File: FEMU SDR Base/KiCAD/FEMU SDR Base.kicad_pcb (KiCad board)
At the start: 4 copper layers, 164.8 x 164.8 mm, 29 parts, among them P8 Raspi_Power_Shield, U1 TPS562209, U2 SDR_1_LDO_1_2V, U3 SDR_2_LDO_1_2V, U4 SDR_1_LDO_3_3V, U5 SDR_2_LDO_3_3V

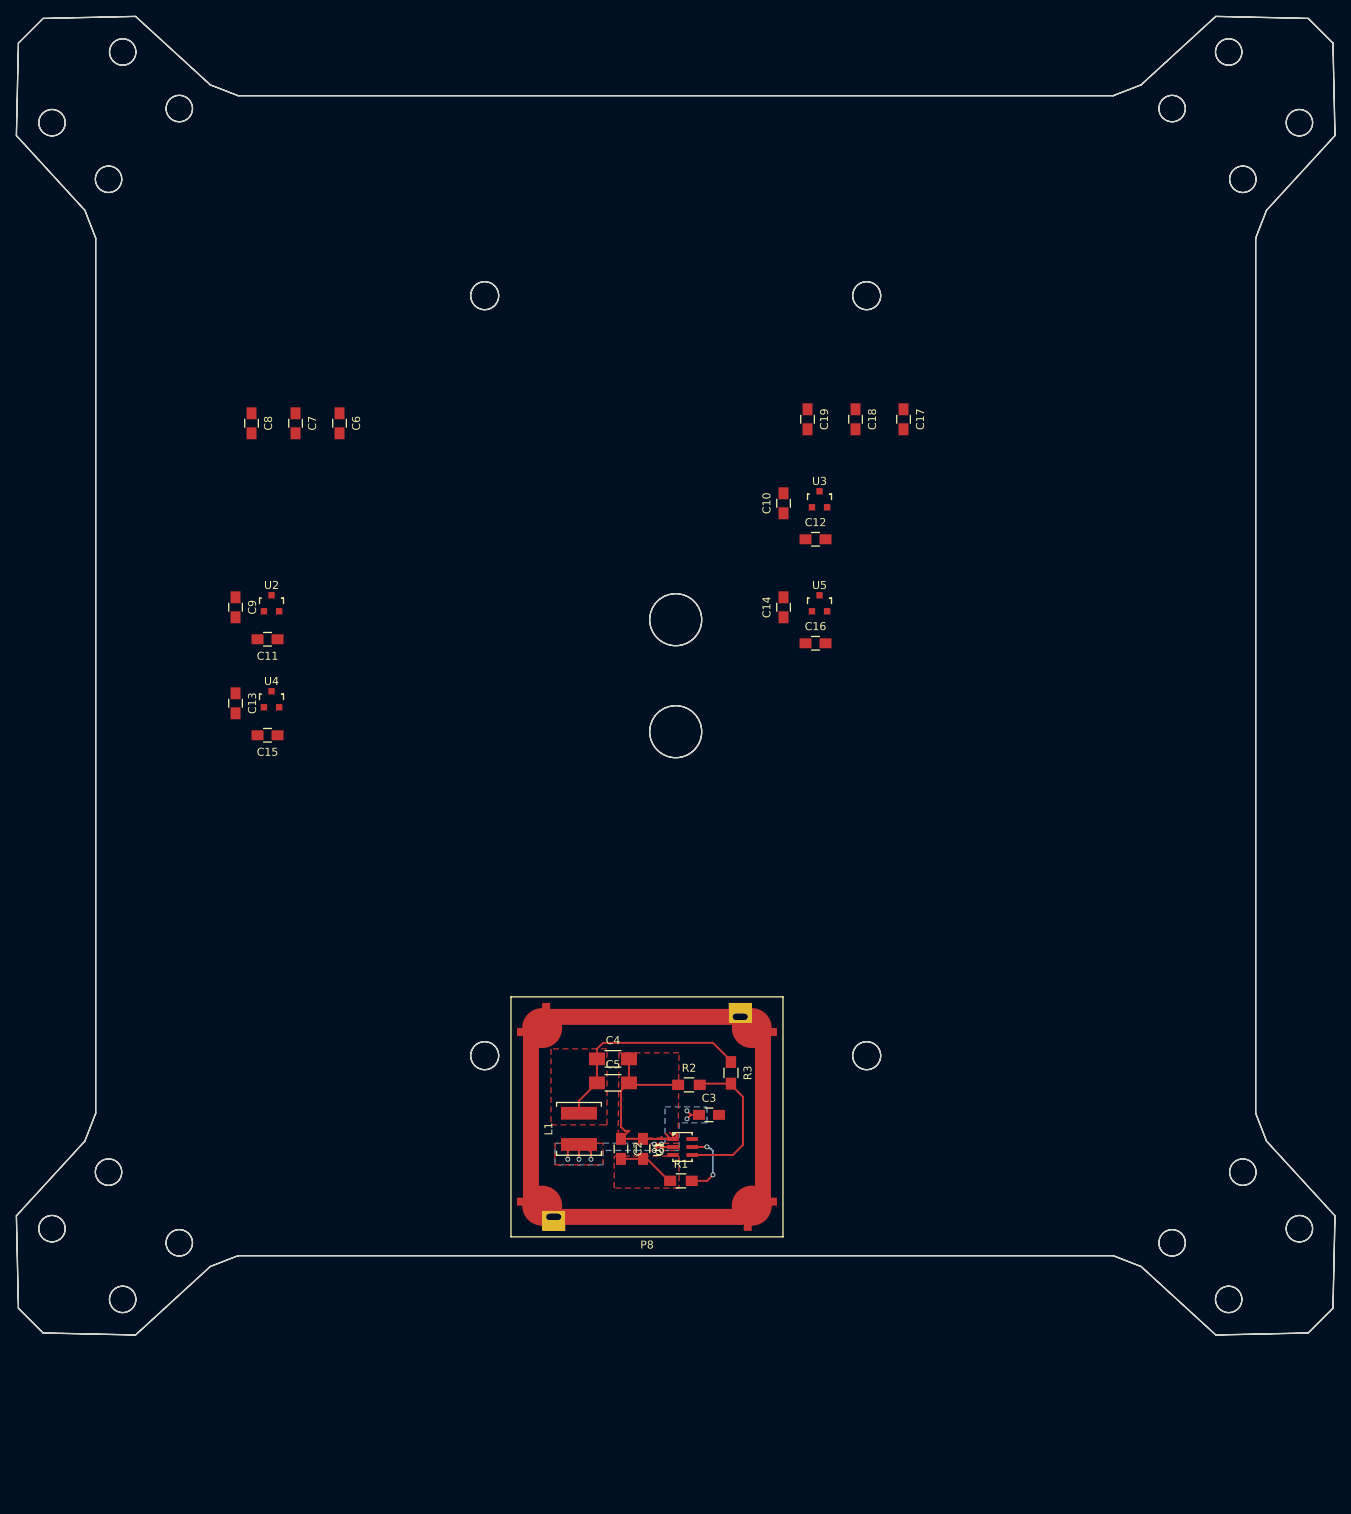
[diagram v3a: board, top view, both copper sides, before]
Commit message: Added SDR shield footprint, updated raspi shield footprints
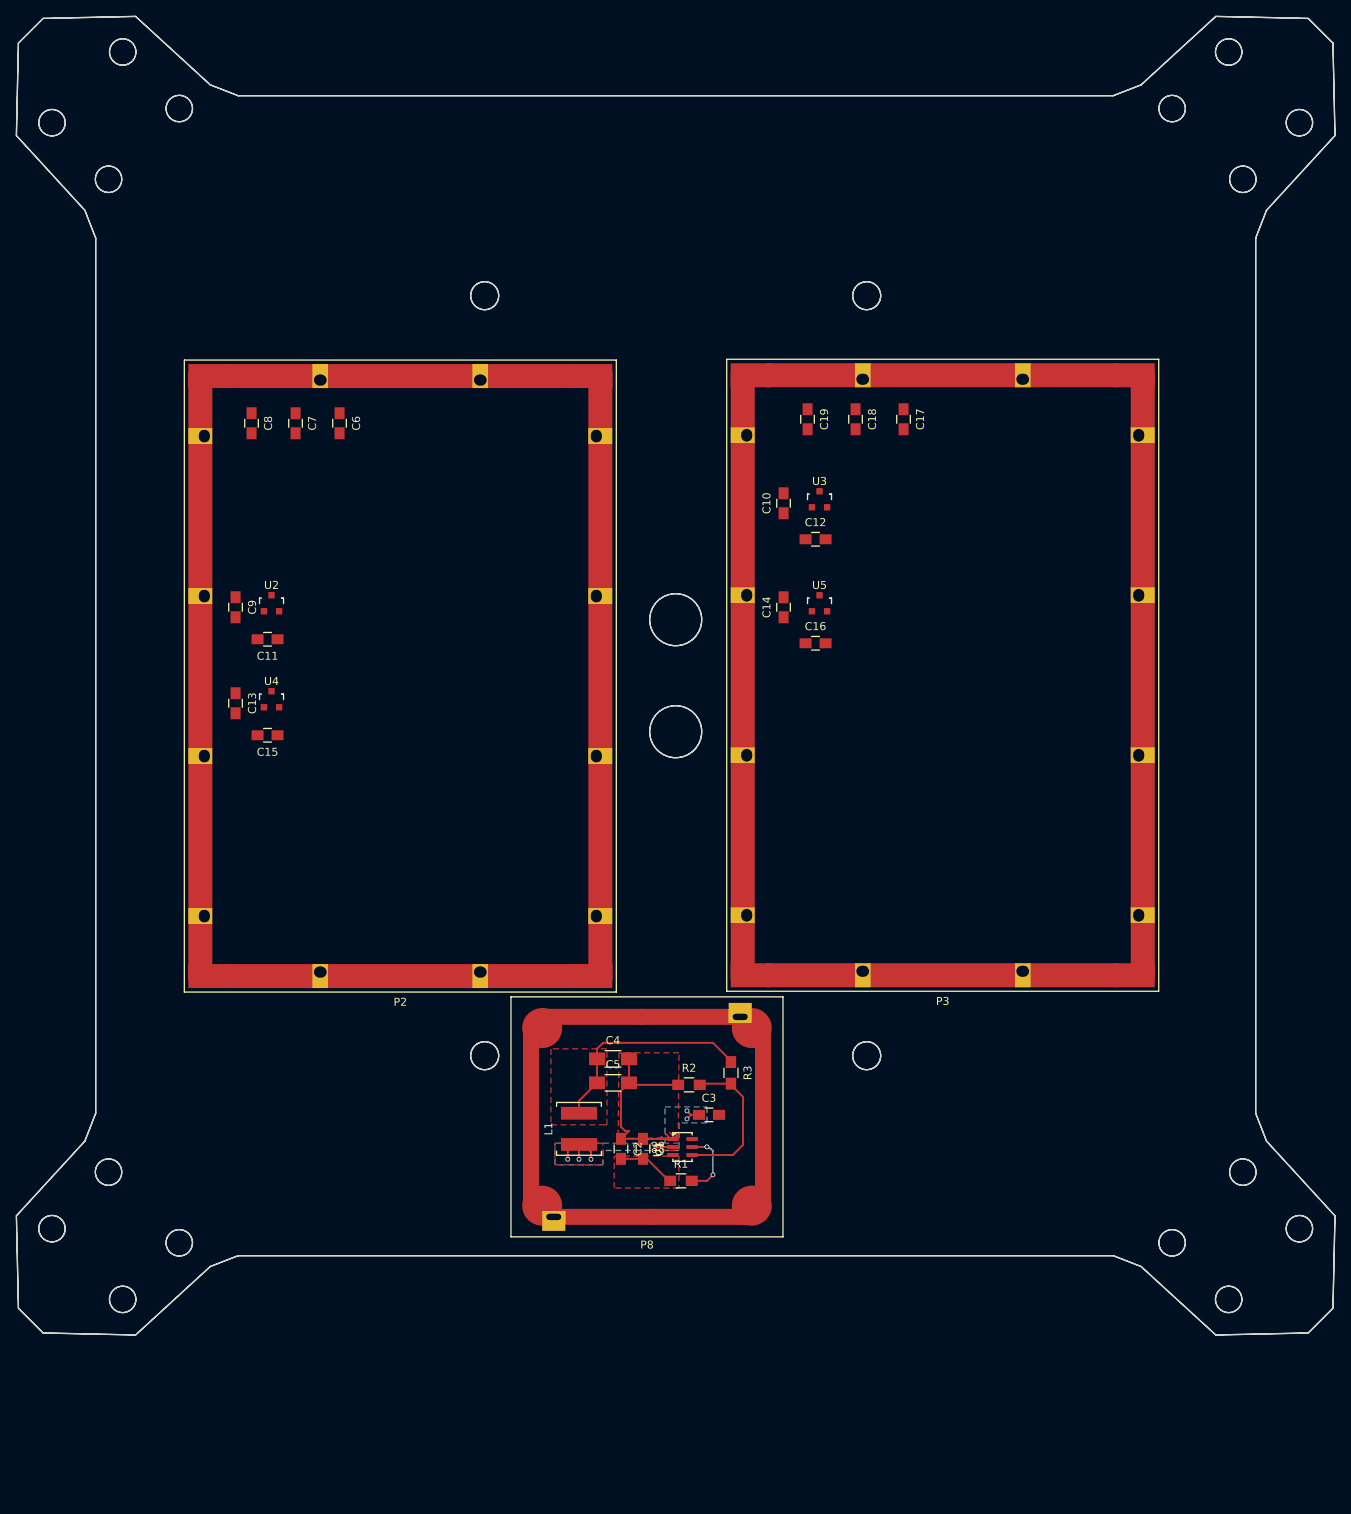
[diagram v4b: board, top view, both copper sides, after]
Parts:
- added P2: SDR_Shield_1, ARB_foots:SDR_Shield_75x50mm, F.Cu at (50.1, 84.6)
- added P3: SDR_Shield_2, ARB_foots:SDR_Shield_75x50mm, F.Cu at (117.9, 84.5)
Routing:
- net GND: track 99.8 -> 10.7 mm

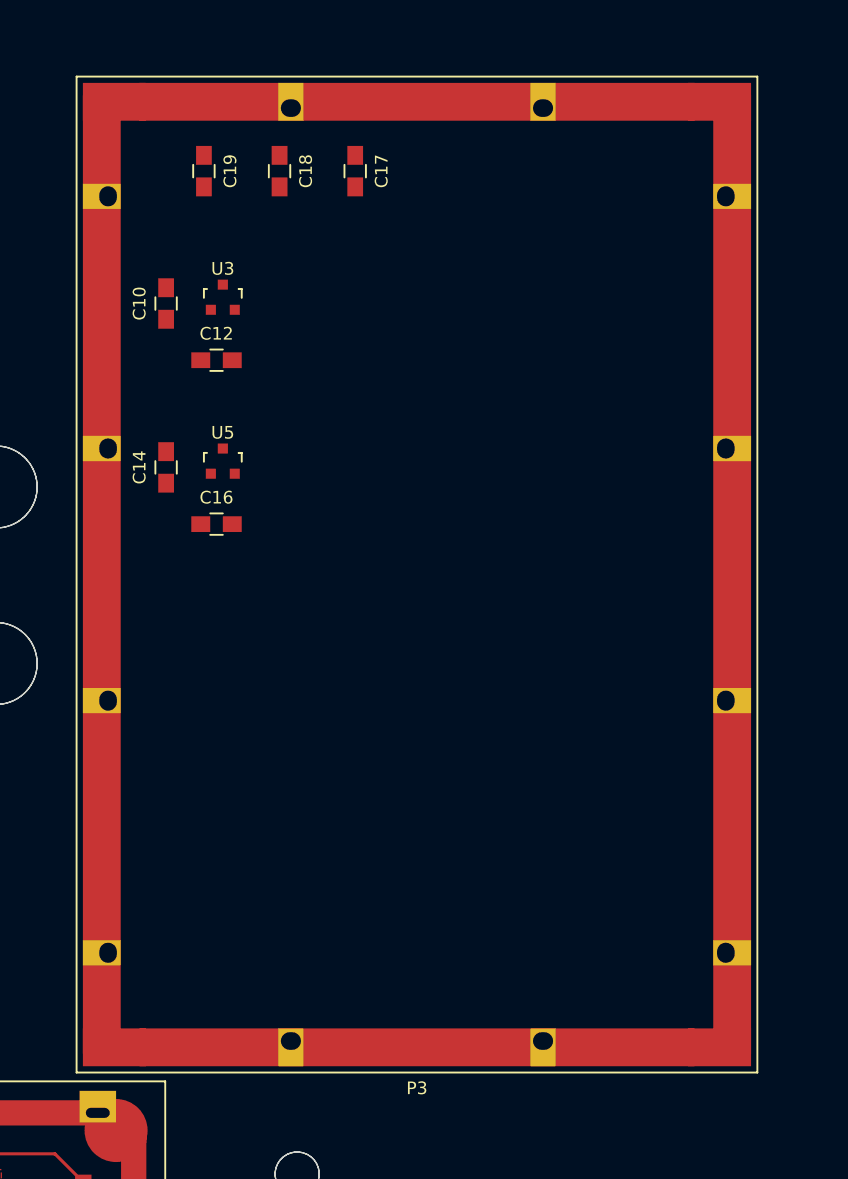
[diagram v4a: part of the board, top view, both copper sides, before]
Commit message: STATUS=FREE, shifted one sdr footprint
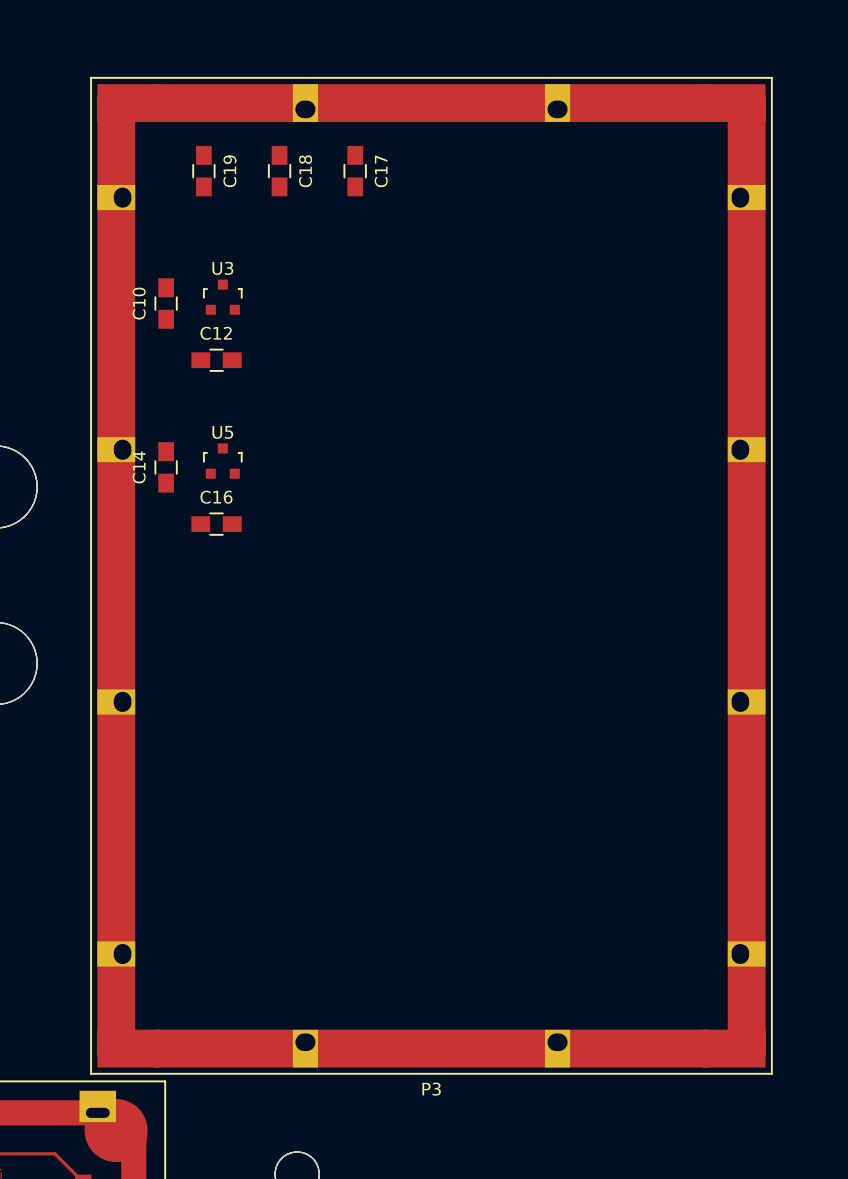
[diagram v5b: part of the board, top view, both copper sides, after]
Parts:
- moved P3 1.15 mm to (119.0, 84.6)
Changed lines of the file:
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@@
     (links 260)
     (no_connects 179)
-    (area 2.059561 2.092061 166.982639 167.015139)
+    (area -15.999999 2.092061 187 174.700001)
     (thickness 1.6)
     (drawings 250)
@@
   )
   (module ARB_foots:SDR_Shield_75x50mm (layer F.Cu)
-    (at 117.9 84.5)
+    (at 119.05 84.6)
     (fp_text reference P3 (at 0 40.75) (layer F.SilkS)
       (effects (font (size 1 1) (thickness 0.15)))

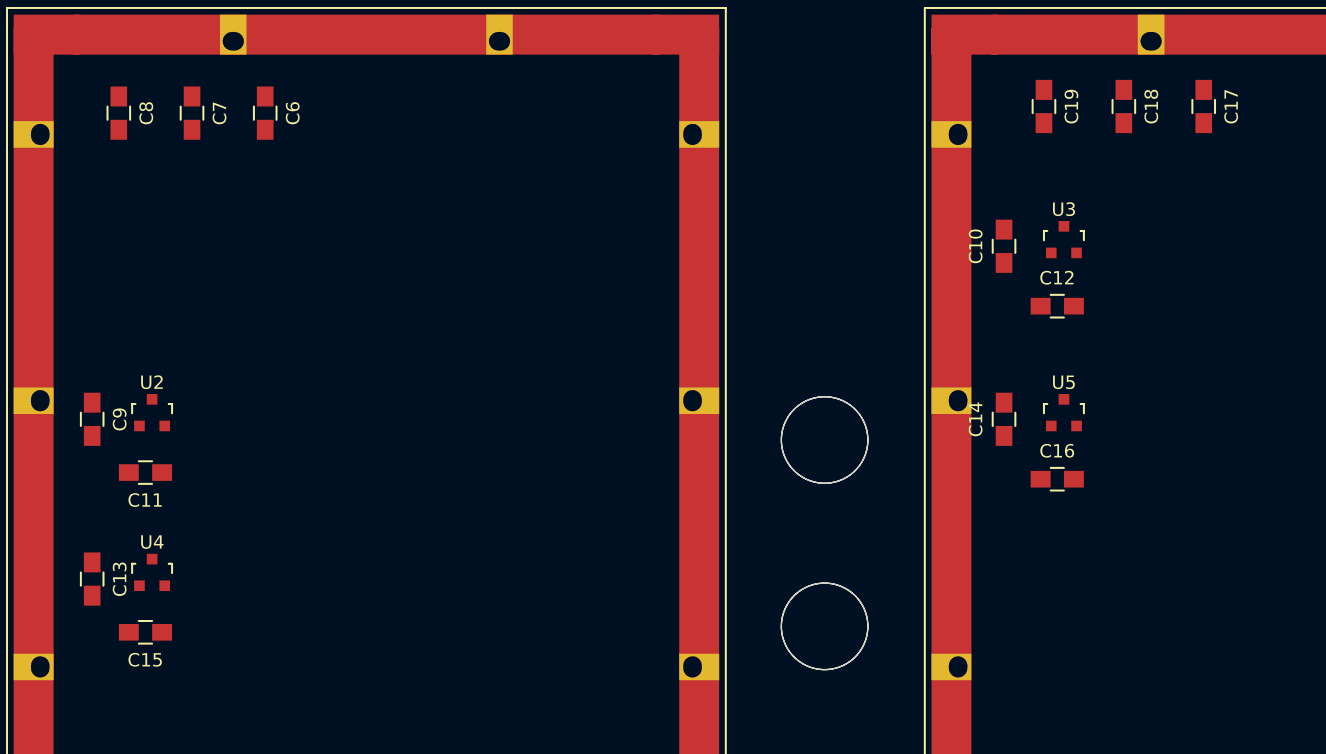
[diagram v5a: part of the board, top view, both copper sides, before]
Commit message: rearranged components in SDR shield footrpint
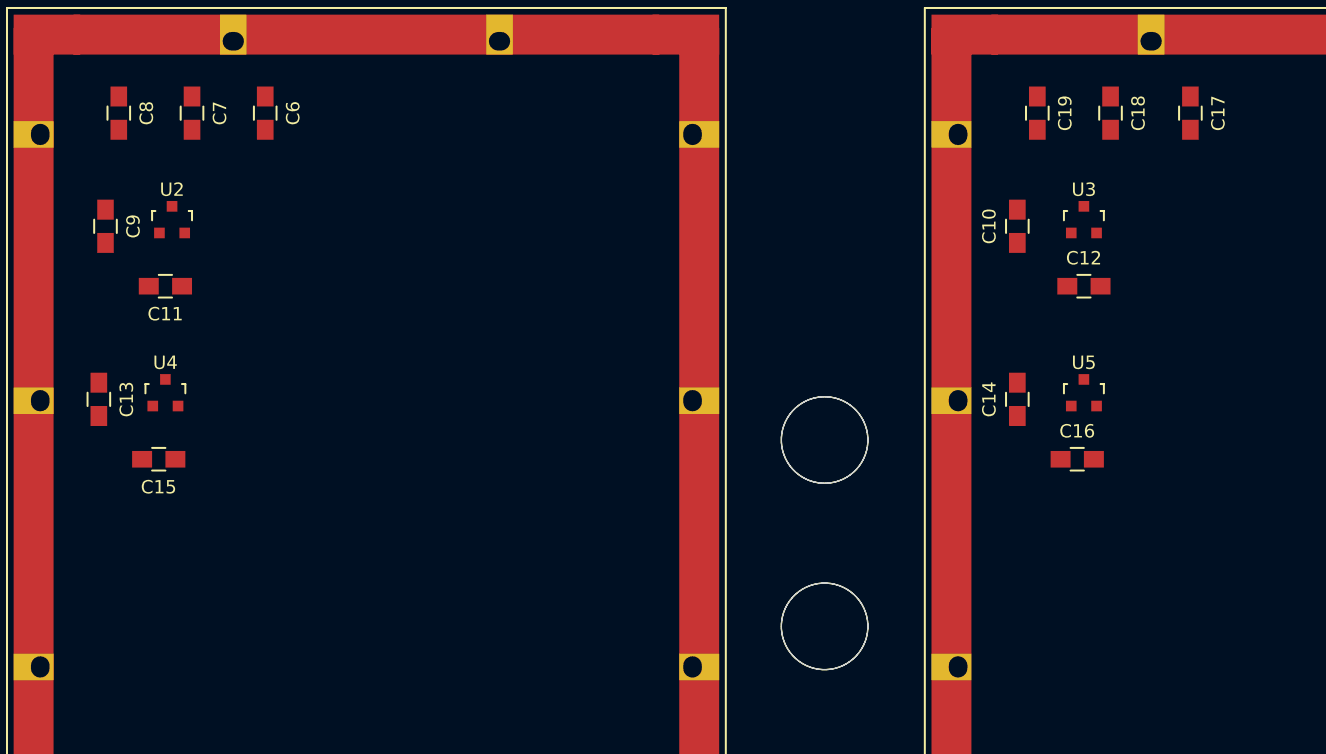
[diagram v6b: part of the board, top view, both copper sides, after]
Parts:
- moved U2 14.6 mm to (35.5, 61.0)
- moved C9 14.5 mm to (30.5, 61.5)
- moved C11 14.1 mm to (35.0, 66.0)
- moved U4 13.5 mm to (35.0, 74.0)
- moved C13 13.5 mm to (30.0, 74.5)
- moved C15 13.0 mm to (34.5, 79.0)
- moved C12 2.50 mm to (104.0, 66.0)
- moved C16 2.12 mm to (103.5, 79.0)
- moved U3 2.12 mm to (104.0, 61.0)
- moved U5 2.12 mm to (104.0, 74.0)
- moved C10 1.80 mm to (99.0, 61.5)
- moved C14 1.80 mm to (99.0, 74.5)
- moved C17 1.12 mm to (112.0, 53.0)
- moved C18 1.12 mm to (106.0, 53.0)
- moved C19 0.71 mm to (100.5, 53.0)
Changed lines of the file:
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@@
   )
   (module TO_SOT_Packages_SMD:SOT-23 (layer F.Cu)
-    (at 34 75.5)
+    (at 35.5 61)
     (descr "SOT-23, Standard")
     (tags SOT-23)
@@
   )
   (module TO_SOT_Packages_SMD:SOT-23 (layer F.Cu)
-    (at 102.5 62.5)
+    (at 104 61)
     (descr "SOT-23, Standard")
     (tags SOT-23)
@@
       (effects (font (size 1 1) (thickness 0.15)))
     )
-    (fp_text value SDR_2_LDO_1_2V (at 0 -5) (layer F.Fab)
+    (fp_text value SDR_2_LDO_1_2V (at 0 -4) (layer F.Fab)
       (effects (font (size 1 1) (thickness 0.15)))
     )
@@
   )
   (module TO_SOT_Packages_SMD:SOT-23 (layer F.Cu)
-    (at 34 87.5)
+    (at 35 74)
     (descr "SOT-23, Standard")
     (tags SOT-23)
@@
   )
   (module TO_SOT_Packages_SMD:SOT-23 (layer F.Cu)
-    (at 102.5 75.5)
+    (at 104 74)
     (descr "SOT-23, Standard")
     (tags SOT-23)
@@
       (effects (font (size 1 1) (thickness 0.15)))
     )
-    (fp_text value SDR_2_LDO_3_3V (at 0 -4.5) (layer F.Fab)
+    (fp_text value SDR_2_LDO_3_3V (at 0 -4) (layer F.Fab)
       (effects (font (size 1 1) (thickness 0.15)))
     )
@@
   )
   (module Capacitors_SMD:C_0805_HandSoldering (layer F.Cu)
-    (at 29.5 76 270)
+    (at 30.5 61.5 270)
     (descr "Capacitor SMD 0805, hand soldering")
     (tags "capacitor 0805")
@@
   )
   (module Capacitors_SMD:C_0805_HandSoldering (layer F.Cu)
-    (at 98 63 90)
+    (at 99 61.5 90)
     (descr "Capacitor SMD 0805, hand soldering")
     (tags "capacitor 0805")
@@
   )
   (module Capacitors_SMD:C_0805_HandSoldering (layer F.Cu)
-    (at 33.5 80 180)
+    (at 35 66 180)
     (descr "Capacitor SMD 0805, hand soldering")
     (tags "capacitor 0805")
@@
   )
   (module Capacitors_SMD:C_0805_HandSoldering (layer F.Cu)
-    (at 102 67.5)
+    (at 104 66)
     (descr "Capacitor SMD 0805, hand soldering")
     (tags "capacitor 0805")
@@
   )
   (module Capacitors_SMD:C_0805_HandSoldering (layer F.Cu)
-    (at 29.5 88 270)
+    (at 30 74.5 270)
     (descr "Capacitor SMD 0805, hand soldering")
     (tags "capacitor 0805")
@@
   )
   (module Capacitors_SMD:C_0805_HandSoldering (layer F.Cu)
-    (at 98 76 90)
+    (at 99 74.5 90)
     (descr "Capacitor SMD 0805, hand soldering")
     (tags "capacitor 0805")
@@
   )
   (module Capacitors_SMD:C_0805_HandSoldering (layer F.Cu)
-    (at 33.5 92 180)
+    (at 34.5 79 180)
     (descr "Capacitor SMD 0805, hand soldering")
     (tags "capacitor 0805")
@@
   )
   (module Capacitors_SMD:C_0805_HandSoldering (layer F.Cu)
-    (at 102 80.5)
+    (at 103.5 79)
     (descr "Capacitor SMD 0805, hand soldering")
     (tags "capacitor 0805")
@@
   )
   (module Capacitors_SMD:C_0805_HandSoldering (layer F.Cu)
-    (at 113 52.5 270)
+    (at 112 53 270)
     (descr "Capacitor SMD 0805, hand soldering")
     (tags "capacitor 0805")
@@
   )
   (module Capacitors_SMD:C_0805_HandSoldering (layer F.Cu)
-    (at 107 52.5 270)
+    (at 106 53 270)
     (descr "Capacitor SMD 0805, hand soldering")
     (tags "capacitor 0805")
@@
   )
   (module Capacitors_SMD:C_0805_HandSoldering (layer F.Cu)
-    (at 101 52.5 270)
-    (descr "Capacitor SMD 0805, hand soldering")
-    (tags "capacitor 0805")
+    (at 100.5 53 270)
+    (descr "Capacitor SMD 0805, hand soldering")
+    (tags "capacitor 0805")
